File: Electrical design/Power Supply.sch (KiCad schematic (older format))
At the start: 21 parts

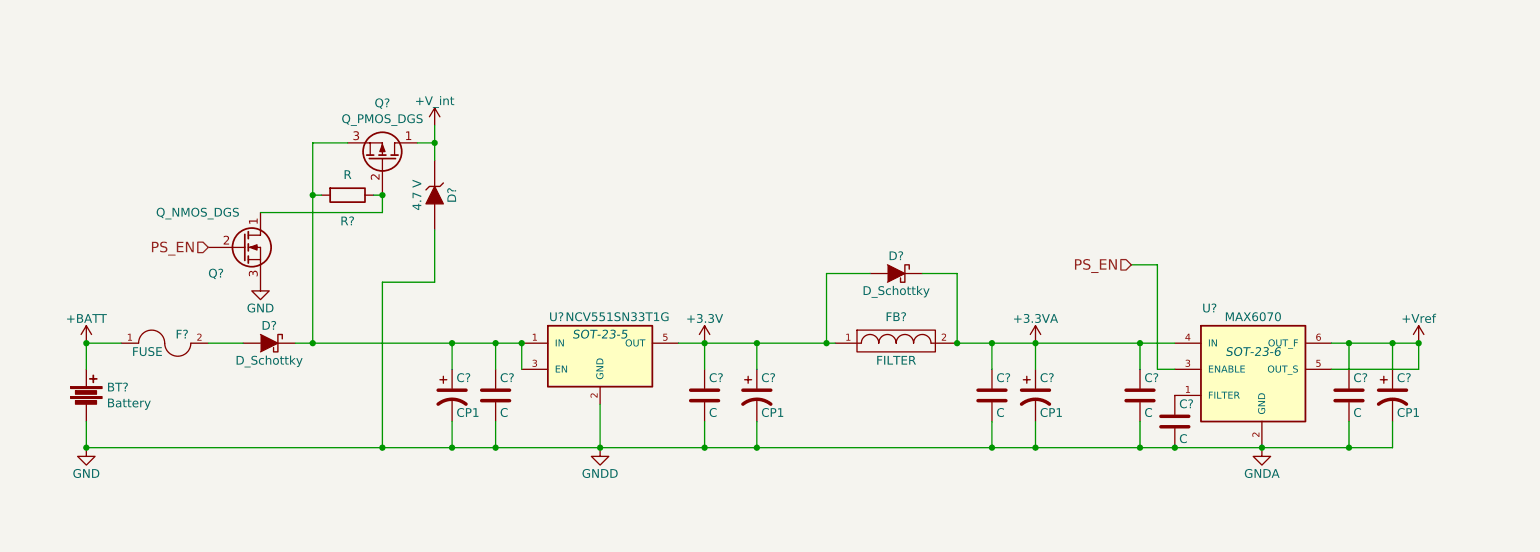
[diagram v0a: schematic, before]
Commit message: Updated schematics.
Added speaker / buzzer, reset circuit (battery under-voltage lockout), changed battery charger IC.
Altered Vout circuit.
Added most resistor / capacitor values (those missing are either dependent on battery thermistor or ADC).
Updated to show "correct" op-amps.
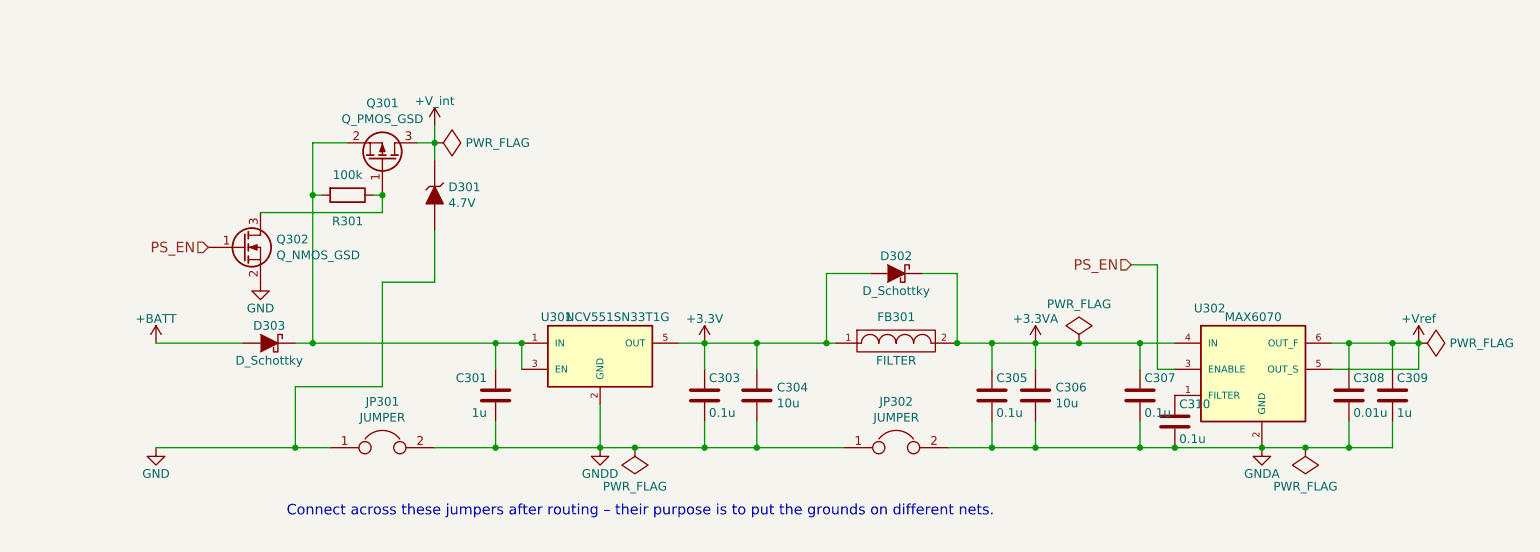
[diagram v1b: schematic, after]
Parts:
- removed BT?: Battery, symbol Battery
- removed C?: C, symbol C
- removed C? (x4): CP1, symbol CP1
- removed D?: 4.7 V, symbol ZENER
- removed F?: FUSE, symbol FUSE
- removed Q?: Q_PMOS_DGS, symbol Q_PMOS_DGS
- removed Q?: Q_NMOS_DGS, symbol Q_NMOS_DGS
- added C301, C309: 1u, my footprints:SMDuniversal_0603to1210_HandSoldering, symbol C
- added C304, C306: 10u, my footprints:SMDuniversal_0603to1210_HandSoldering, symbol C
- added D301: 4.7V, TO_SOT_Packages_SMD:SOT-23, symbol ZENER_SOT23
- added JP301, JP302: JUMPER, Resistors_SMD:R_0201, symbol JUMPER
- added Q301: Q_PMOS_GSD, TO_SOT_Packages_SMD:SOT-23, symbol Q_PMOS_GSD
- added Q302: Q_NMOS_GSD, TO_SOT_Packages_SMD:SOT-23, symbol Q_NMOS_GSD
- C303, C305, C307, C310: renamed from C?; value C -> 0.1u; footprint (none) -> my footprints:SMDuniversal_0603to1210_HandSoldering
- C308: renamed from C?; value C -> 0.01u; footprint (none) -> my footprints:SMDuniversal_0603to1210_HandSoldering
- D302, D303: renamed from D?; footprint (none) -> my footprints:SC-90A
- FB301: renamed from FB?; footprint (none) -> my footprints:SMDuniversal_0603to1210_HandSoldering
- R301: renamed from R?; value R -> 100k; footprint (none) -> my footprints:SMDuniversal_0603to1210_HandSoldering
- U301: renamed from U?; footprint SOT-23-5 -> TO_SOT_Packages_SMD:SOT-23-5
- U302: renamed from U?; footprint SOT-23-6 -> TO_SOT_Packages_SMD:SOT-23-6_Handsoldering
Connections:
- net +3.3VA: now also C306.1
- net +3V3: now also C304.1
- net +BATT: now also D303.2 (A)
- net +V_int: now also D301.3 (K), Q301.3 (D)
- net +Vref: now also C309.1
- net GND: now also D301.1 (A), JP301.1, Q302.2 (S); no longer C303.2, C305.2, C307.2, C308.2, C310.2, U301.2 (GND), U302.2 (GND)
- net PS_EN: now also Q302.1 (G)
- net at D303.1 (K), R301.2, U301.1 (IN)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: now also C301.1, Q301.2 (S)
- net at R301.1: now also Q301.1 (G), Q302.3 (D)
- new net GNDA: C305.2, C306.2, C307.2, C308.2, C309.2, C310.2, JP302.2, U302.2 (GND)
- new net GNDD: C301.2, C303.2, C304.2, JP301.2, JP302.1, U301.2 (GND)
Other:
- note added: "Connect across these jumpers after routing – their purpose is to put the grounds on different nets."

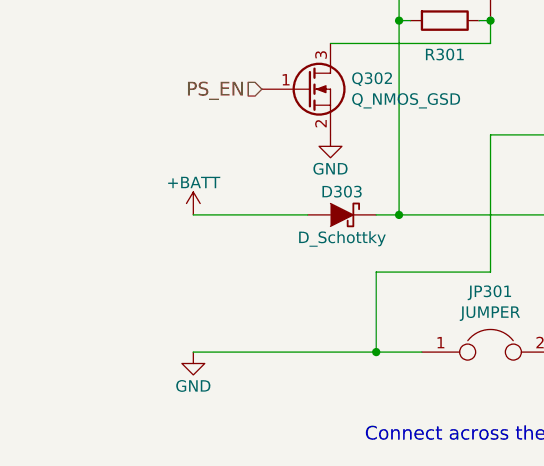
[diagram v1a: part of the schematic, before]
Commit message: Add battery voltage monitoring.
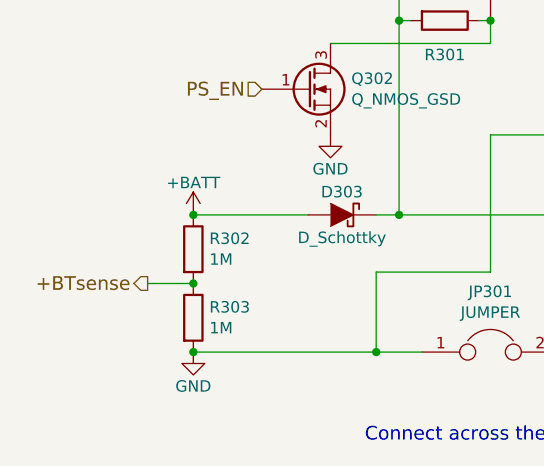
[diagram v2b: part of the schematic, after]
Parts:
- added R302, R303: 1M, my footprints:SMDuniversal_0603to1210_HandSoldering, symbol R
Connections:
- net +BATT: now also R302.1
- net GND: now also R303.2
- new net +BTsense: R302.2, R303.1
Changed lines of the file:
@@
 $EndComp
 $Comp
-L +BATT #PWR303
+L +BATT #PWR051
 U 1 1 5739B8CC
 P 2300 3350
-F 0 "#PWR303" H 2300 3200 50  0001 C CNN
+F 0 "#PWR051" H 2300 3200 50  0001 C CNN
 F 1 "+BATT" H 2300 3490 50  0000 C CNN
 F 2 "" H 2300 3350 50  0000 C CNN
@@
 $EndComp
 $Comp
-L +3.3V #PWR304
+L +3.3V #PWR052
 U 1 1 5739B8E6
 P 5450 3350
-F 0 "#PWR304" H 5450 3200 50  0001 C CNN
+F 0 "#PWR052" H 5450 3200 50  0001 C CNN
 F 1 "+3.3V" H 5450 3490 50  0000 C CNN
 F 2 "" H 5450 3350 50  0000 C CNN
@@
 $EndComp
 $Comp
-L +V_int #PWR301
+L +V_int #PWR053
 U 1 1 5739B900
 P 3900 2100
-F 0 "#PWR301" H 3900 1950 50  0001 C CNN
+F 0 "#PWR053" H 3900 1950 50  0001 C CNN
 F 1 "+V_int" H 3900 2240 50  0000 C CNN
 F 2 "" H 3900 2100 50  0000 C CNN
@@
 $EndComp
 $Comp
-L +Vref #PWR306
+L +Vref #PWR054
 U 1 1 5739B91A
 P 9550 3350
-F 0 "#PWR306" H 9550 3200 50  0001 C CNN
+F 0 "#PWR054" H 9550 3200 50  0001 C CNN
 F 1 "+Vref" H 9550 3490 50  0000 C CNN
 F 2 "" H 9550 3350 50  0000 C CNN
@@
 $EndComp
 $Comp
-L GND #PWR307
+L GND #PWR055
 U 1 1 5739BDEB
 P 2300 3950
-F 0 "#PWR307" H 2300 3700 50  0001 C CNN
+F 0 "#PWR055" H 2300 3700 50  0001 C CNN
 F 1 "GND" H 2300 3800 50  0000 C CNN
 F 2 "" H 2300 3950 50  0000 C CNN
@@
 $EndComp
 $Comp
-L GNDA #PWR309
+L GNDA #PWR056
 U 1 1 5739C20D
 P 8650 3950
-F 0 "#PWR309" H 8650 3700 50  0001 C CNN
+F 0 "#PWR056" H 8650 3700 50  0001 C CNN
 F 1 "GNDA" H 8650 3800 50  0000 C CNN
 F 2 "" H 8650 3950 50  0000 C CNN
@@
 $EndComp
 $Comp
-L GNDD #PWR308
+L GNDD #PWR057
 U 1 1 5739C227
 P 4850 3950
-F 0 "#PWR308" H 4850 3700 50  0001 C CNN
+F 0 "#PWR057" H 4850 3700 50  0001 C CNN
 F 1 "GNDD" H 4850 3800 50  0000 C CNN
 F 2 "" H 4850 3950 50  0000 C CNN
@@
 $EndComp
 $Comp
-L +3.3VA #PWR305
+L +3.3VA #PWR058
 U 1 1 5739C474
 P 7350 3350
-F 0 "#PWR305" H 7350 3200 50  0001 C CNN
+F 0 "#PWR058" H 7350 3200 50  0001 C CNN
 F 1 "+3.3VA" H 7350 3490 50  0000 C CNN
 F 2 "" H 7350 3350 50  0000 C CNN
@@
 $EndComp
 $Comp
-L GND #PWR302
+L GND #PWR059
 U 1 1 574BA199
 P 2900 3000
-F 0 "#PWR302" H 2900 2750 50  0001 C CNN
+F 0 "#PWR059" H 2900 2750 50  0001 C CNN
 F 1 "GND" H 2900 2850 50  0000 C CNN
 F 2 "" H 2900 3000 50  0000 C CNN
@@
 $EndComp
 $Comp
-L PWR_FLAG #FLG304
+L PWR_FLAG #FLG060
 U 1 1 5767E1D0
 P 5050 3950
-F 0 "#FLG304" H 5050 4045 50  0001 C CNN
+F 0 "#FLG060" H 5050 4045 50  0001 C CNN
 F 1 "PWR_FLAG" H 5050 4173 50  0000 C CNN
 F 2 "" H 5050 3950 50  0000 C CNN
@@
 $EndComp
 $Comp
-L PWR_FLAG #FLG305
+L PWR_FLAG #FLG061
 U 1 1 5767E20E
 P 8900 3950
-F 0 "#FLG305" H 8900 4045 50  0001 C CNN
+F 0 "#FLG061" H 8900 4045 50  0001 C CNN
 F 1 "PWR_FLAG" H 8900 4173 50  0000 C CNN
 F 2 "" H 8900 3950 50  0000 C CNN
@@
 $EndComp
 $Comp
-L PWR_FLAG #FLG301
+L PWR_FLAG #FLG062
 U 1 1 5767E74E
 P 3900 2200
-F 0 "#FLG301" H 3900 2295 50  0001 C CNN
+F 0 "#FLG062" H 3900 2295 50  0001 C CNN
 F 1 "PWR_FLAG" V 3900 2378 50  0000 L CNN
 F 2 "" H 3900 2200 50  0000 C CNN
@@
 $EndComp
 $Comp
-L PWR_FLAG #FLG303
+L PWR_FLAG #FLG063
 U 1 1 5767E862
 P 9550 3350
-F 0 "#FLG303" H 9550 3445 50  0001 C CNN
+F 0 "#FLG063" H 9550 3445 50  0001 C CNN
 F 1 "PWR_FLAG" V 9550 3528 50  0000 L CNN
 F 2 "" H 9550 3350 50  0000 C CNN
@@
 $EndComp
 $Comp
-L PWR_FLAG #FLG302
+L PWR_FLAG #FLG064
 U 1 1 5767E89C
 P 7600 3350
-F 0 "#FLG302" H 7600 3445 50  0001 C CNN
+F 0 "#FLG064" H 7600 3445 50  0001 C CNN
 F 1 "PWR_FLAG" H 7600 3574 50  0000 C CNN
 F 2 "" H 7600 3350 50  0000 C CNN
@@
 Connection ~ 8900 3950
 Connection ~ 7600 3350
+$Comp
+L R R303
+U 1 1 5769169A
+P 2300 3800
+F 0 "R303" H 2370 3846 50  0000 L CNN
+F 1 "1M" H 2370 3755 50  0000 L CNN
+F 2 "my footprints:SMDuniversal_0603to1210_HandSoldering" V 2230 3800 50  0001 C CNN
+F 3 "" H 2300 3800 50  0000 C CNN
+	1    2300 3800
+	1    0    0    -1
+$EndComp
+$Comp
+L R R302
+U 1 1 576916E6
+P 2300 3500
+F 0 "R302" H 2370 3546 50  0000 L CNN
+F 1 "1M" H 2370 3455 50  0000 L CNN
+F 2 "my footprints:SMDuniversal_0603to1210_HandSoldering" V 2230 3500 50  0001 C CNN
+F 3 "" H 2300 3500 50  0000 C CNN
+	1    2300 3500
+	1    0    0    -1
+$EndComp
+Connection ~ 2300 3350
+Connection ~ 2300 3950
+Connection ~ 2300 3650
+Text HLabel 2100 3650 0    60   Output ~ 0
++BTsense
+Wire Wire Line
+	2100 3650 2300 3650
 $EndSCHEMATC

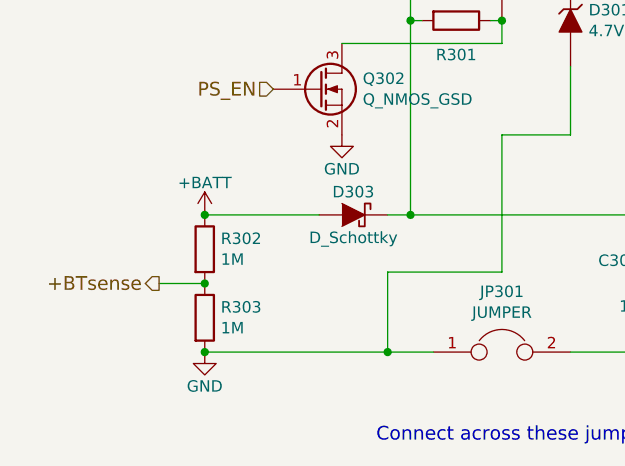
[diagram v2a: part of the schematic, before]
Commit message: Update External Design. Add battery sense capacitor. Update footprints.
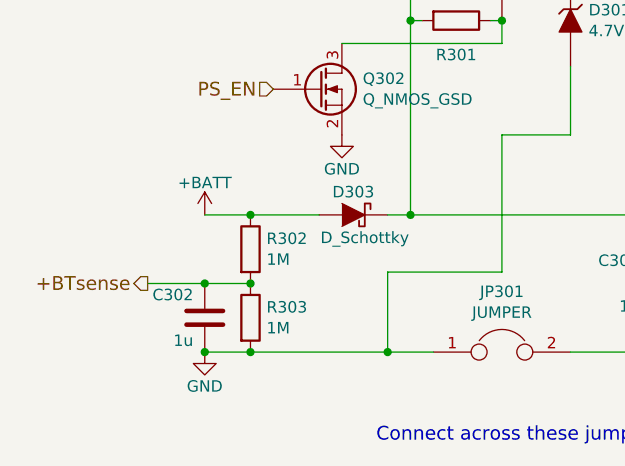
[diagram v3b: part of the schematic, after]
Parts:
- added C302: 1u, my footprints:SMDuniversal_0603to0805_HandSoldering, symbol C
- C301, C303, C305, C307, C308, C309, C310: footprint my footprints:SMDuniversal_0603to1210_HandSoldering -> my footprints:SMDuniversal_0603to0805_HandSoldering
- C304, C306: footprint my footprints:SMDuniversal_0603to1210_HandSoldering -> my footprints:SMDuniversal_0603to1206_HandSoldering
- JP301, JP302: footprint Resistors_SMD:R_0201 -> Resistors_SMD:R_0805
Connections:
- net +BTsense: now also C302.1
- net GND: now also C302.2
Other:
- moved on the sheet: R302, R303
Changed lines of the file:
@@
 Sheet 3 5
 Title "Power supply"
-Date ""
-Rev ""
+Date "2016-06-22"
+Rev "0.5"
 Comp ""
 Comment1 ""
@@
 F 0 "C303" H 5475 3750 50  0000 L CNN
 F 1 "0.1u" H 5475 3550 50  0000 L CNN
-F 2 "my footprints:SMDuniversal_0603to1210_HandSoldering" H 5488 3500 50  0001 C CNN
+F 2 "my footprints:SMDuniversal_0603to0805_HandSoldering" H 5488 3500 50  0001 C CNN
 F 3 "" H 5450 3650 50  0000 C CNN
 	1    5450 3650
@@
 F 0 "C310" H 8175 3900 50  0000 L CNN
 F 1 "0.1u" H 8175 3700 50  0000 L CNN
-F 2 "my footprints:SMDuniversal_0603to1210_HandSoldering" H 8188 3650 50  0001 C CNN
+F 2 "my footprints:SMDuniversal_0603to0805_HandSoldering" H 8188 3650 50  0001 C CNN
 F 3 "" H 8150 3800 50  0000 C CNN
 	1    8150 3800
@@
 F 0 "C307" H 7975 3750 50  0000 L CNN
 F 1 "0.1u" H 7975 3550 50  0000 L CNN
-F 2 "my footprints:SMDuniversal_0603to1210_HandSoldering" H 7988 3500 50  0001 C CNN
+F 2 "my footprints:SMDuniversal_0603to0805_HandSoldering" H 7988 3500 50  0001 C CNN
 F 3 "" H 7950 3650 50  0000 C CNN
 	1    7950 3650
@@
 F 0 "C305" H 7125 3750 50  0000 L CNN
 F 1 "0.1u" H 7125 3550 50  0000 L CNN
-F 2 "my footprints:SMDuniversal_0603to1210_HandSoldering" H 7138 3500 50  0001 C CNN
+F 2 "my footprints:SMDuniversal_0603to0805_HandSoldering" H 7138 3500 50  0001 C CNN
 F 3 "" H 7100 3650 50  0000 C CNN
 	1    7100 3650
@@
 F 0 "C308" H 9175 3750 50  0000 L CNN
 F 1 "0.01u" H 9175 3550 50  0000 L CNN
-F 2 "my footprints:SMDuniversal_0603to1210_HandSoldering" H 9188 3500 50  0001 C CNN
+F 2 "my footprints:SMDuniversal_0603to0805_HandSoldering" H 9188 3500 50  0001 C CNN
 F 3 "" H 9150 3650 50  0000 C CNN
 	1    9150 3650
@@
 P 2950 3350
 F 0 "D303" H 2950 3450 50  0000 C CNN
-F 1 "D_Schottky" H 2950 3250 50  0000 C CNN
+F 1 "D_Schottky" H 2900 3250 50  0000 C CNN
 F 2 "my footprints:SC-90A" H 2950 3350 50  0001 C CNN
 F 3 "" H 2950 3350 50  0000 C CNN
@@
 F 0 "JP301" H 3600 4214 50  0000 C CNN
 F 1 "JUMPER" H 3600 4123 50  0000 C CNN
-F 2 "Resistors_SMD:R_0201" H 3600 3950 50  0001 C CNN
+F 2 "Resistors_SMD:R_0805" H 3600 3950 50  0001 C CNN
 F 3 "" H 3600 3950 50  0000 C CNN
 	1    3600 3950
@@
 F 0 "JP302" H 6550 4214 50  0000 C CNN
 F 1 "JUMPER" H 6550 4123 50  0000 C CNN
-F 2 "Resistors_SMD:R_0201" H 6550 3950 50  0001 C CNN
+F 2 "Resistors_SMD:R_0805" H 6550 3950 50  0001 C CNN
 F 3 "" H 6550 3950 50  0000 C CNN
 	1    6550 3950
@@
 F 0 "C309" H 9425 3750 50  0000 L CNN
 F 1 "1u" H 9425 3550 50  0000 L CNN
-F 2 "my footprints:SMDuniversal_0603to1210_HandSoldering" H 9438 3500 50  0001 C CNN
+F 2 "my footprints:SMDuniversal_0603to0805_HandSoldering" H 9438 3500 50  0001 C CNN
 F 3 "" H 9400 3650 50  0000 C CNN
 	1    9400 3650
@@
 F 0 "C301" H 4300 3750 50  0000 L CNN
 F 1 "1u" H 4300 3550 50  0000 L CNN
-F 2 "my footprints:SMDuniversal_0603to1210_HandSoldering" H 4288 3500 50  0001 C CNN
+F 2 "my footprints:SMDuniversal_0603to0805_HandSoldering" H 4288 3500 50  0001 C CNN
 F 3 "" H 4250 3650 50  0000 C CNN
 	1    4250 3650
@@
 F 0 "C304" H 5865 3696 50  0000 L CNN
 F 1 "10u" H 5865 3605 50  0000 L CNN
-F 2 "my footprints:SMDuniversal_0603to1210_HandSoldering" H 5788 3500 50  0001 C CNN
+F 2 "my footprints:SMDuniversal_0603to1206_HandSoldering" H 5788 3500 50  0001 C CNN
 F 3 "" H 5750 3650 50  0000 C CNN
 	1    5750 3650
@@
 F 0 "C306" H 7465 3696 50  0000 L CNN
 F 1 "10u" H 7465 3605 50  0000 L CNN
-F 2 "my footprints:SMDuniversal_0603to1210_HandSoldering" H 7388 3500 50  0001 C CNN
+F 2 "my footprints:SMDuniversal_0603to1206_HandSoldering" H 7388 3500 50  0001 C CNN
 F 3 "" H 7350 3650 50  0000 C CNN
 	1    7350 3650
@@
 L R R303
 U 1 1 5769169A
+P 2500 3800
+F 0 "R303" H 2570 3846 50  0000 L CNN
+F 1 "1M" H 2570 3755 50  0000 L CNN
+F 2 "my footprints:SMDuniversal_0603to1210_HandSoldering" V 2430 3800 50  0001 C CNN
+F 3 "" H 2500 3800 50  0000 C CNN
+	1    2500 3800
+	1    0    0    -1
+$EndComp
+$Comp
+L R R302
+U 1 1 576916E6
+P 2500 3500
+F 0 "R302" H 2570 3546 50  0000 L CNN
+F 1 "1M" H 2570 3455 50  0000 L CNN
+F 2 "my footprints:SMDuniversal_0603to1210_HandSoldering" V 2430 3500 50  0001 C CNN
+F 3 "" H 2500 3500 50  0000 C CNN
+	1    2500 3500
+	1    0    0    -1
+$EndComp
+Connection ~ 2300 3950
+Connection ~ 2500 3650
+Text HLabel 2050 3650 0    60   Output ~ 0
++BTsense
+Wire Wire Line
+	2050 3650 2500 3650
+$Comp
+L C C302
+U 1 1 576912EA
 P 2300 3800
-F 0 "R303" H 2370 3846 50  0000 L CNN
-F 1 "1M" H 2370 3755 50  0000 L CNN
-F 2 "my footprints:SMDuniversal_0603to1210_HandSoldering" V 2230 3800 50  0001 C CNN
+F 0 "C302" H 2350 3900 50  0000 L CNN
+F 1 "1u" H 2350 3700 50  0000 L CNN
+F 2 "my footprints:SMDuniversal_0603to0805_HandSoldering" H 2338 3650 50  0001 C CNN
 F 3 "" H 2300 3800 50  0000 C CNN
 	1    2300 3800
-	1    0    0    -1
-$EndComp
-$Comp
-L R R302
-U 1 1 576916E6
-P 2300 3500
-F 0 "R302" H 2370 3546 50  0000 L CNN
-F 1 "1M" H 2370 3455 50  0000 L CNN
-F 2 "my footprints:SMDuniversal_0603to1210_HandSoldering" V 2230 3500 50  0001 C CNN
-F 3 "" H 2300 3500 50  0000 C CNN
-	1    2300 3500
-	1    0    0    -1
-$EndComp
-Connection ~ 2300 3350
-Connection ~ 2300 3950
+	-1   0    0    -1
+$EndComp
 Connection ~ 2300 3650
-Text HLabel 2100 3650 0    60   Output ~ 0
-+BTsense
-Wire Wire Line
-	2100 3650 2300 3650
+Connection ~ 2500 3950
+Connection ~ 2500 3350
 $EndSCHEMATC

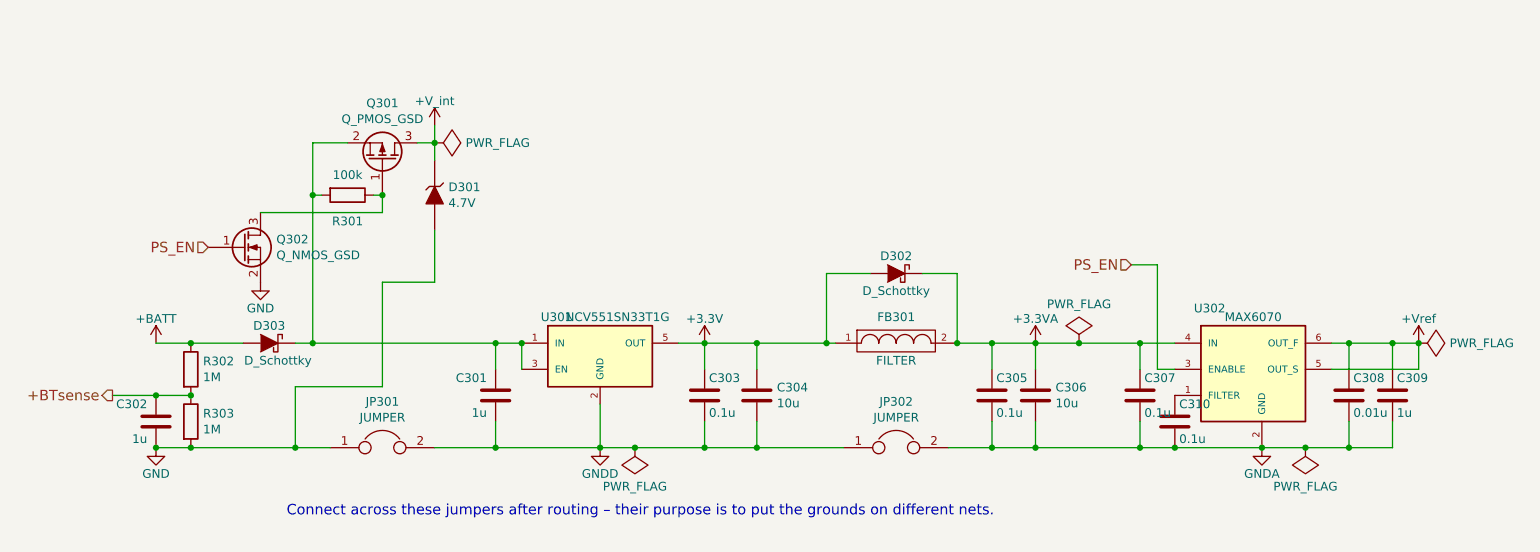
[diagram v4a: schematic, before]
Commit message: Tied ground nets together, fixed clearance issues, added copper pours / zones.
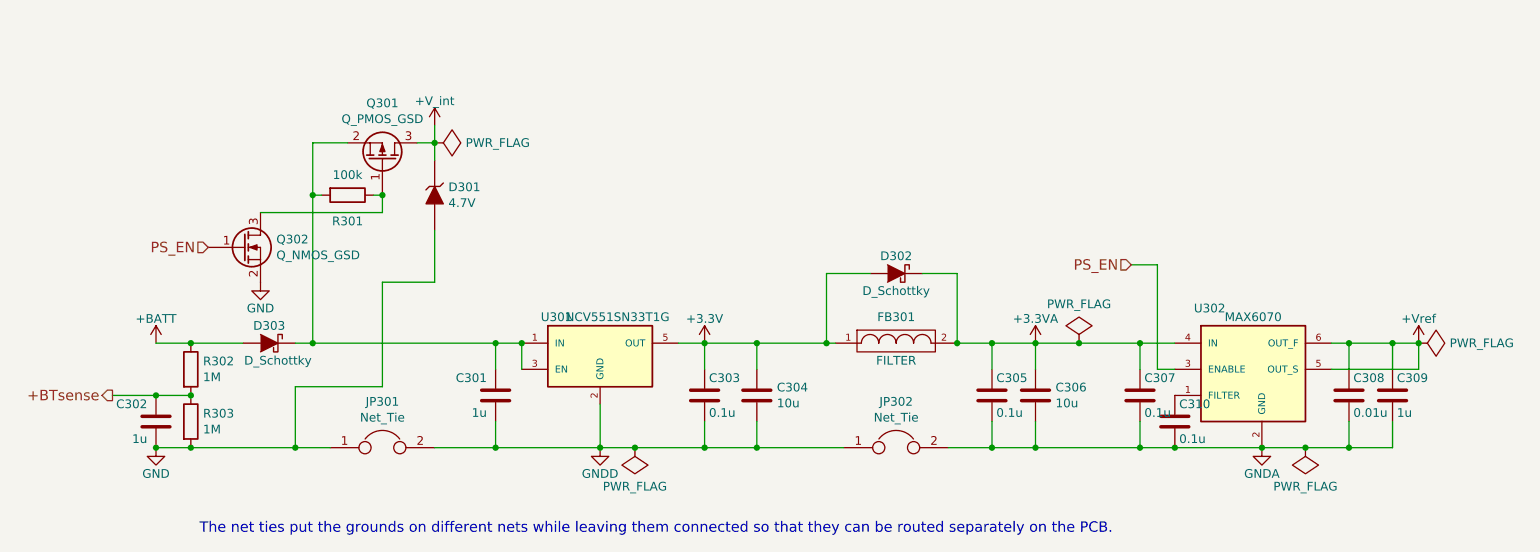
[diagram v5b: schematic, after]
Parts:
- JP301, JP302: value JUMPER -> Net_Tie; footprint Resistors_SMD:R_0805 -> my footprints:Net_Tie
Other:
- note added: "The net ties put the grounds on different nets while leaving them connected so that they can be routed separately on the PCB."
- note removed: "Connect across these jumpers after routing – their purpose is to put the grounds on different nets."
